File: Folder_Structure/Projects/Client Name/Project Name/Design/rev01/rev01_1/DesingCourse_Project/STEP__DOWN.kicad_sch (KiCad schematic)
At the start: 0 parts

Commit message: Update 8
Page 1 finished, INPUT finished, Start of USB-C
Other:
- note removed: "BLOCK DIAGRAM"
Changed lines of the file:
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@@
 		(comment 4 "Josue Godinez")
 	)
-	(text "BLOCK DIAGRAM"
-		(exclude_from_sim no)
-		(at 160.02 20.066 0)
-		(effects
-			(font
-				(face "Arial Black")
-				(size 7.62 7.62)
-				(thickness 0.254)
-				(bold yes)
-				(color 29 0 255 1)
-			)
-		)
-	)
 )

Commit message: Update 9
USC-C & STEP_DOWN are DONE // MCU missing TVS diodes on P3V3 & P5V
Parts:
- added C46, C47, C48, C49: 1u, symbol Device:C
- added D7: BAT60A, Diode_SMD:D_SOD-323, symbol Diode:BAT60A
- added D8, D9: LED_G, symbol Device:LED
- added R43, R44: 1k, symbol Device:R
- added U4: AMS1117-3.3, Package_TO_SOT_SMD:SOT-223-3_TabPin2, symbol Regulator_Linear:AMS1117-3.3
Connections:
- new net: D8.2 (A), R43.2
- new net: D9.2 (A), R44.2
- new net: C48.1, C49.1, D7.2 (A), U4.2 (VO)
- new net GND: C46.2, C47.2, C48.2, C49.2, D8.1 (K), D9.1 (K), U4.1 (GND)
- new net P3V3: D7.1 (K), R44.1
- new net P5V: C46.1, C47.1, R43.1, U4.3 (VI)
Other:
- note added: "FROM MOSFET DRIVER OR EXTERNAL SOURCE"
- note added: "STEP DOWN"

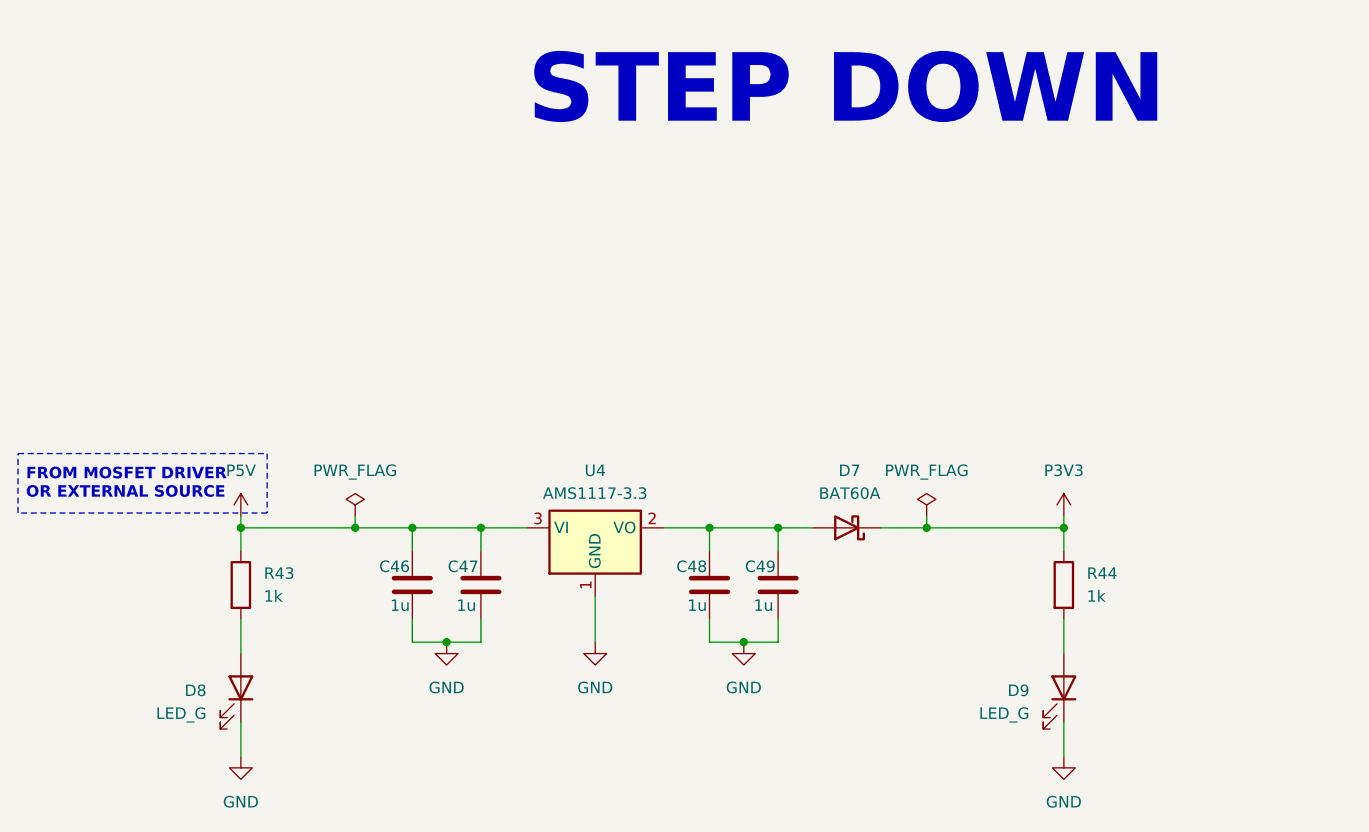
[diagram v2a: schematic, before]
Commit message: Update 12
Until STEP-DOWN page, all components have complete libraries.

Creation and incluison of all logos and labels libraries
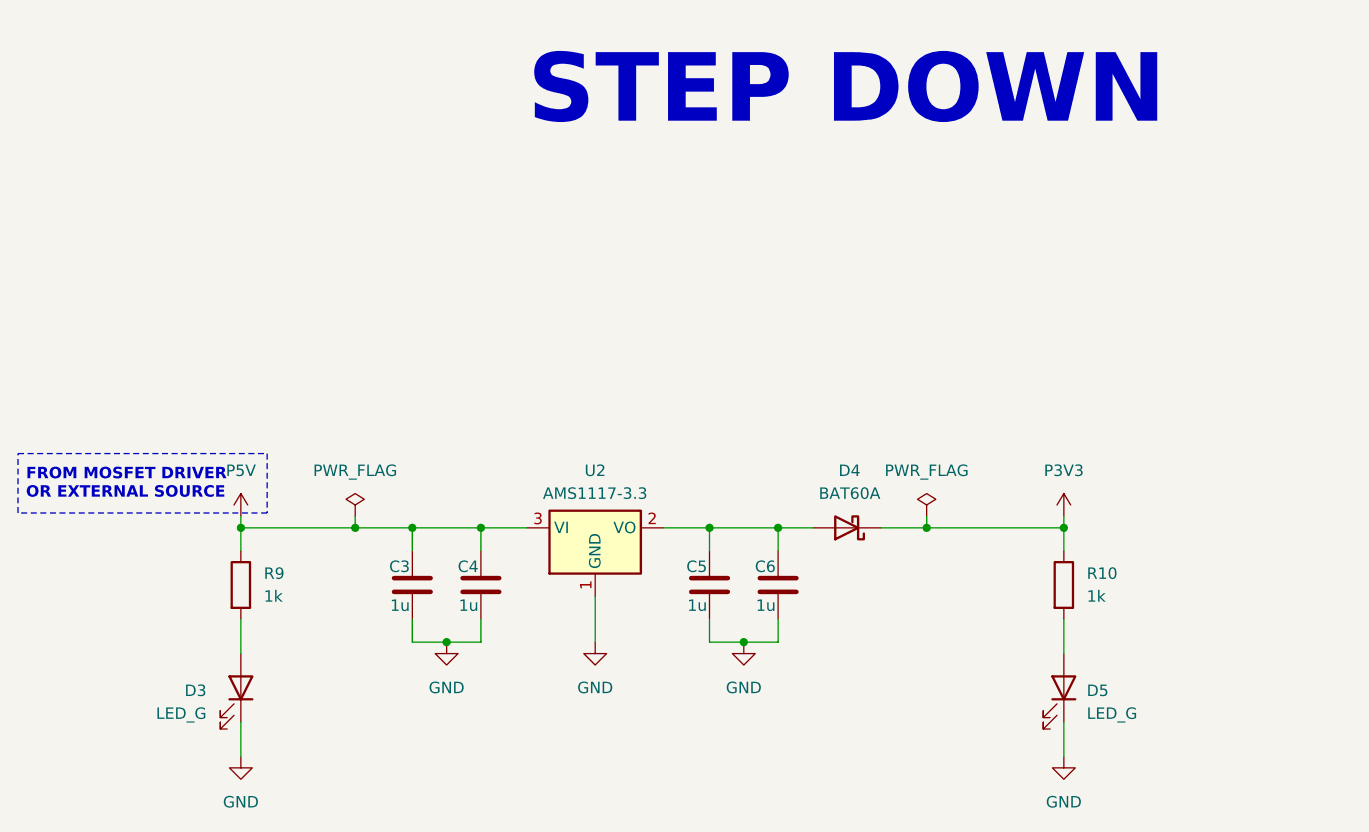
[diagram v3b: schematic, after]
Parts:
- removed C47, C48, C49: 1u, symbol Device:C
- removed D8, D9: LED_G, symbol Device:LED
- removed R43, R44: 1k, symbol Device:R
- added C4, C5, C6: 1u, Capacitor_SMD:C_0603_1608Metric, symbol Device:C
- added D3, D5: LED_G, Diode_SMD:D_1206_3216Metric, symbol Device:LED
- added R10, R9: 1k, Resistor_SMD:R_0603_1608Metric, symbol Device:R
- C3: renamed from C46; footprint (none) -> Capacitor_SMD:C_0603_1608Metric; Package (none) -> 0603; Temp Coeff (none) -> X5R; Tolerance (none) -> 10%; Voltage Rating (none) -> 10V
- D4: renamed from D7; MPN (none) -> BAT60A; Manufacturer (none) -> Infineon; Package (none) -> SOD-323
- U2: renamed from U4; MPN (none) -> AMS1117-3.3; Manufacturer (none) -> Advanced Monolithic Systems; Package (none) -> 3pin SOT-223
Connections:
- net GND: now also C4.2, C5.2, C6.2, D3.1 (K), D5.1 (K)
- net P3V3: now also R10.1
- net P5V: now also C4.1, R9.1
- net at D4.2 (A), U2.2 (VO): now also C5.1, C6.1
- new net: D3.2 (A), R9.2
- new net: D5.2 (A), R10.2

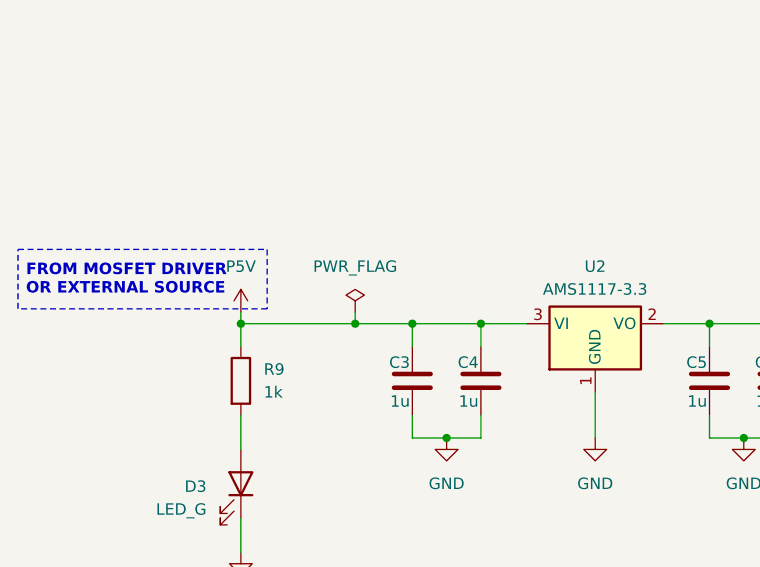
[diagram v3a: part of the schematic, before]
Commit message: Update 16
Initial component placement done
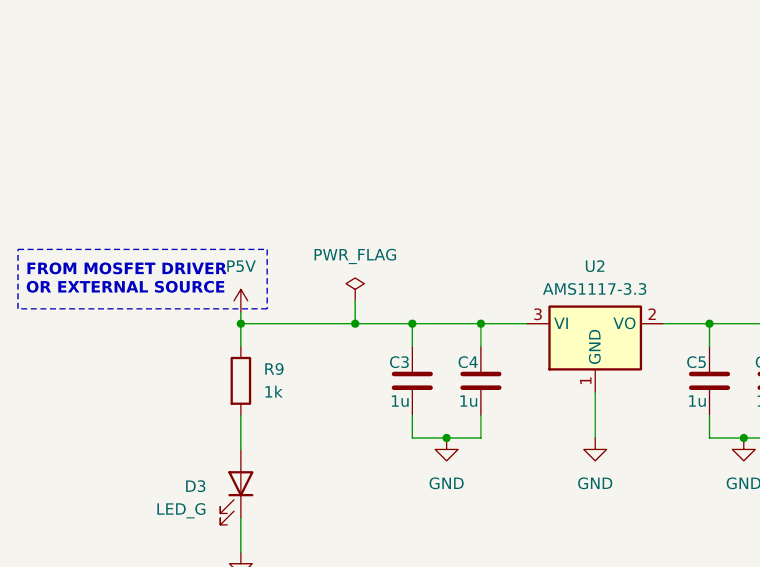
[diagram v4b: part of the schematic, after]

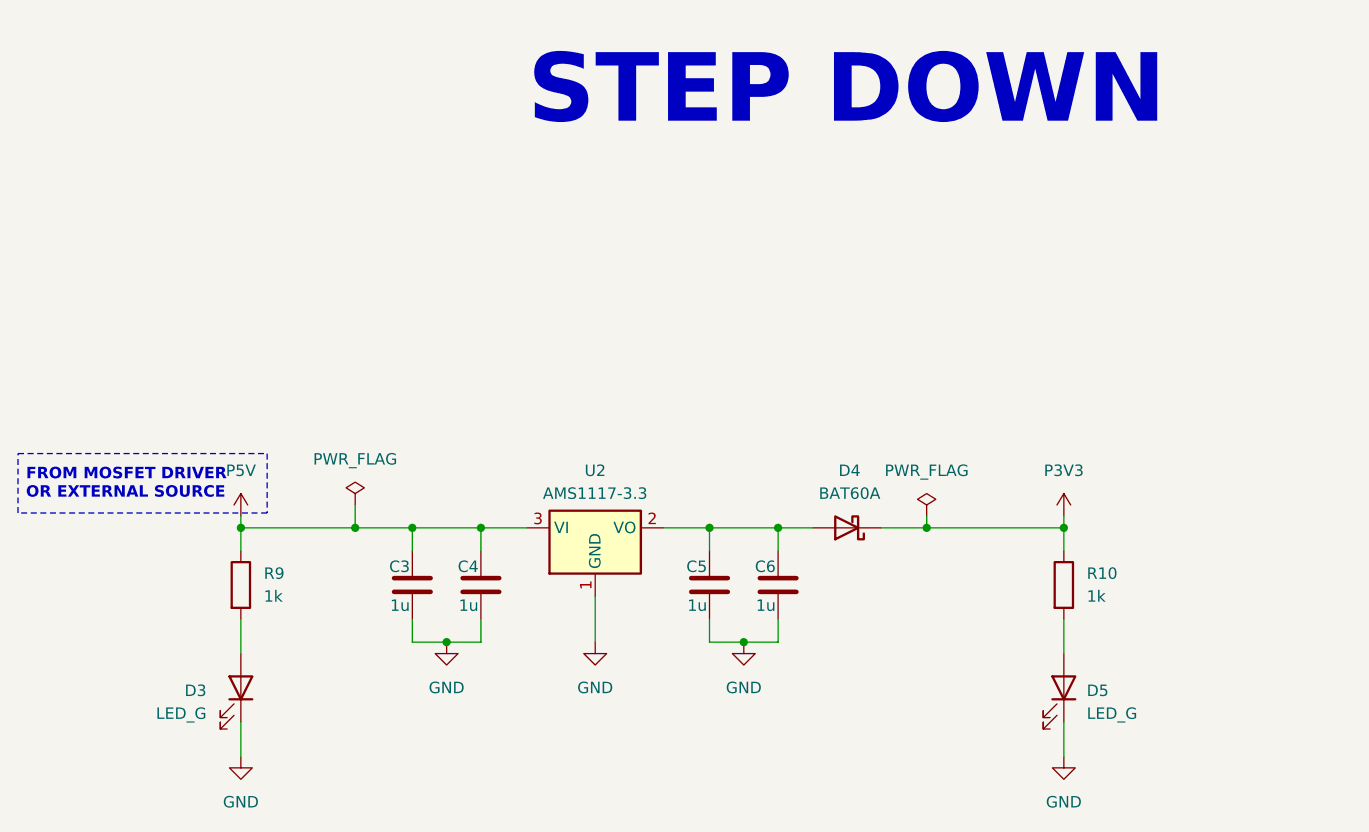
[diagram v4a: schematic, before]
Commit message: Update17
Design rules and stack defined.

Check againg DR and proceed with layout.
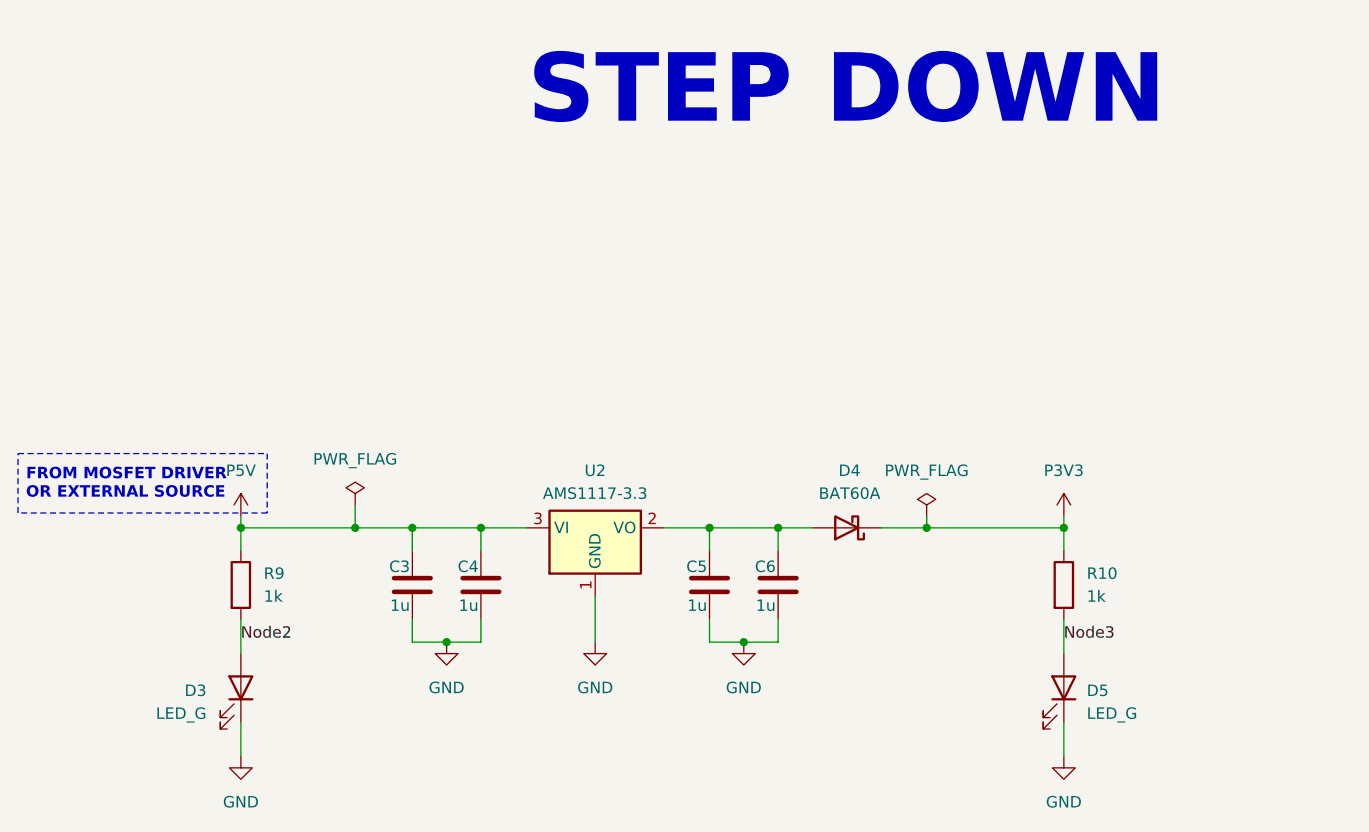
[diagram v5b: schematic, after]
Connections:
- net Node2: now reaches D3.2 (A), R9.2
- net Node3: now reaches D5.2 (A), R10.2
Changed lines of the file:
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@@
+		)
+	)
+	(label "Node3"
+		(at 184.15 81.28 0)
+		(effects
+			(font
+				(size 1.27 1.27)
+			)
+			(justify left bottom)
+		)
+	)
+	(label "Node2"
+		(at 92.71 81.28 0)
+		(effects
+			(font
+				(size 1.27 1.27)
+			)
+			(justify left bottom)
 		)
 	)

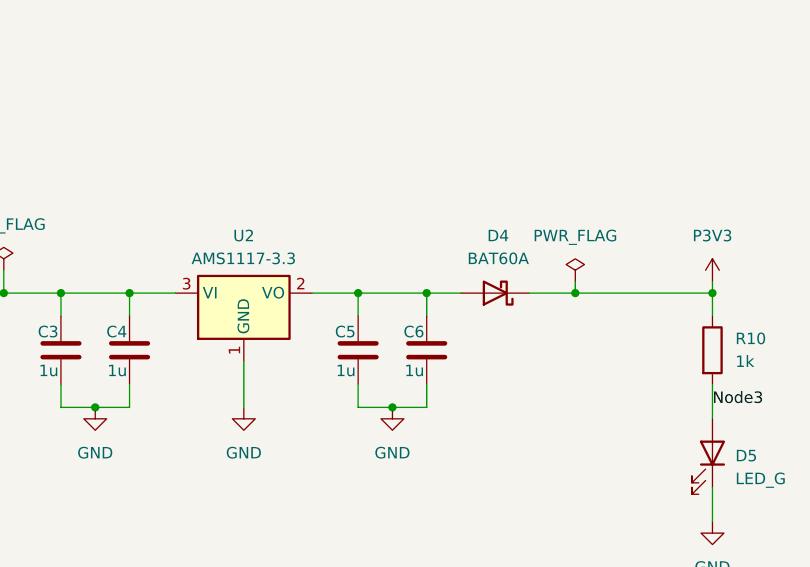
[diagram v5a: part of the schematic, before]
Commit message: Update18
Layout finished, clean up or layout and designators.
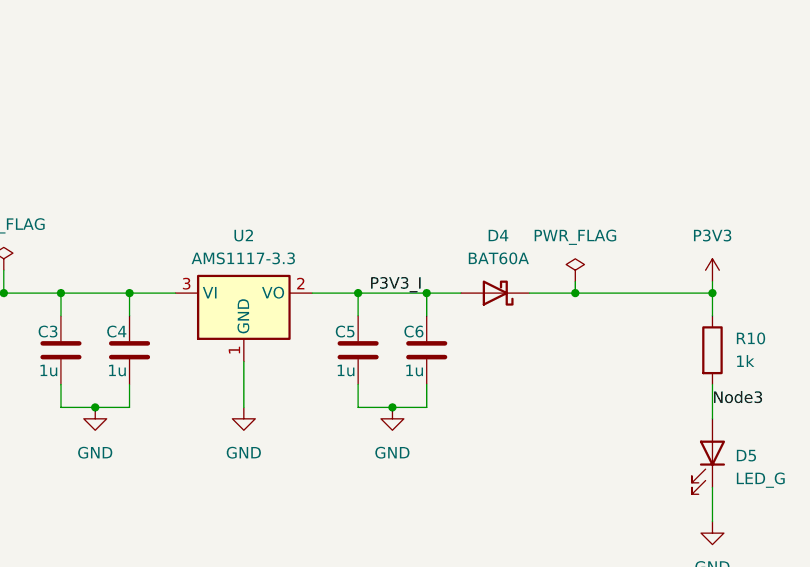
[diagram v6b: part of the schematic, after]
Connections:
- net P3V3_I: now reaches C5.1, C6.1, D4.2 (A), U2.2 (VO)
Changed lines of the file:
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@@
+		)
+	)
+	(label "P3V3_I"
+		(at 146.05 68.58 0)
+		(effects
+			(font
+				(size 1.27 1.27)
+			)
+			(justify left bottom)
 		)
 	)
@@
 			)
 		)
-		(property "Description" "CAP CER 1UF 10V X5R 0603"
+		(property "Description" "Unpolarized capacitor"
 			(at 152.4 74.93 0)
 			(effects
@@
 			)
 		)
-		(property "Description" "CAP CER 1UF 10V X5R 0603"
+		(property "Description" "Unpolarized capacitor"
 			(at 144.78 74.93 0)
 			(effects
@@
 			)
 		)
-		(property "Description" "LED GREEN CLEAR 1206 SMD"
+		(property "Description" "Light emitting diode"
 			(at 92.71 86.36 0)
 			(effects
@@
 			)
 		)
-		(property "Description" "RES 1k OHM 0603 ±1% 1/10W"
+		(property "Description" "Resistor"
 			(at 92.71 74.93 0)
 			(effects
@@
 			)
 		)
-		(property "Description" "LED GREEN CLEAR 1206 SMD"
+		(property "Description" "Light emitting diode"
 			(at 184.15 86.36 0)
 			(effects
@@
 			)
 		)
-		(property "Description" "RES 1k OHM 0603 ±1% 1/10W"
+		(property "Description" "Resistor"
 			(at 184.15 74.93 0)
 			(effects
@@
 			)
 		)
-		(property "Description" "CAP CER 1UF 10V X5R 0603"
+		(property "Description" "Unpolarized capacitor"
 			(at 119.38 74.93 0)
 			(effects
@@
 			)
 		)
-		(property "Description" "CAP CER 1UF 10V X5R 0603"
+		(property "Description" "Unpolarized capacitor"
 			(at 111.76 74.93 0)
 			(effects
